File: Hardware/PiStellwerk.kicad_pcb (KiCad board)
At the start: 2 copper layers, 65 x 56 mm, 89 parts, among them J1 Conn_02x20_Odd_Even, J2 Screw_Terminal_01x02, J3 Screw_Terminal_01x02, J6 Conn_01x01, J7 Conn_01x04, J8 Conn_01x06, J9 Conn_01x05, Q1 Q_PMOS_GDS, U1 STM32F103C8Tx, U2 HT7533, U3 DRV8876, U4 SY8303, U5 ADUM4160, U6 ISO3088DW, U7 SY8303, U8 SY8303, U9 SY8303

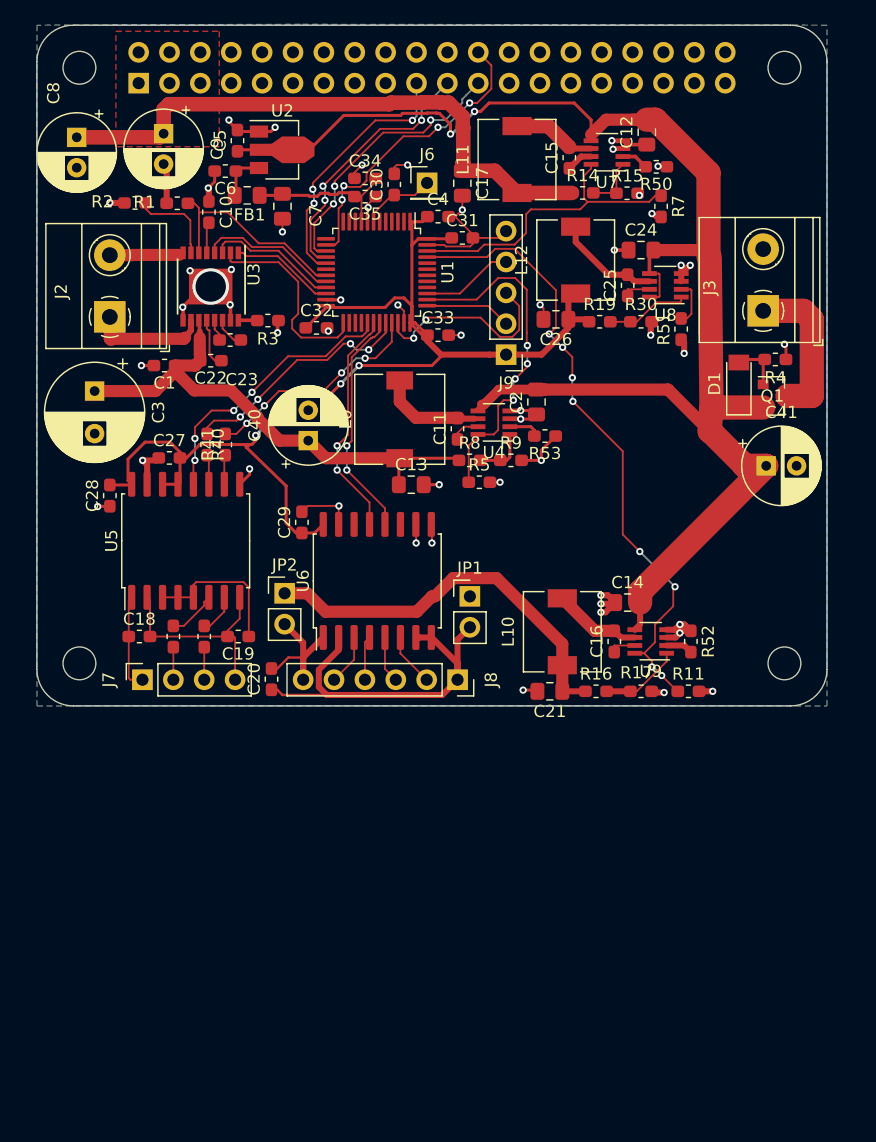
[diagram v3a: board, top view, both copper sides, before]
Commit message: initial work on 4layer design
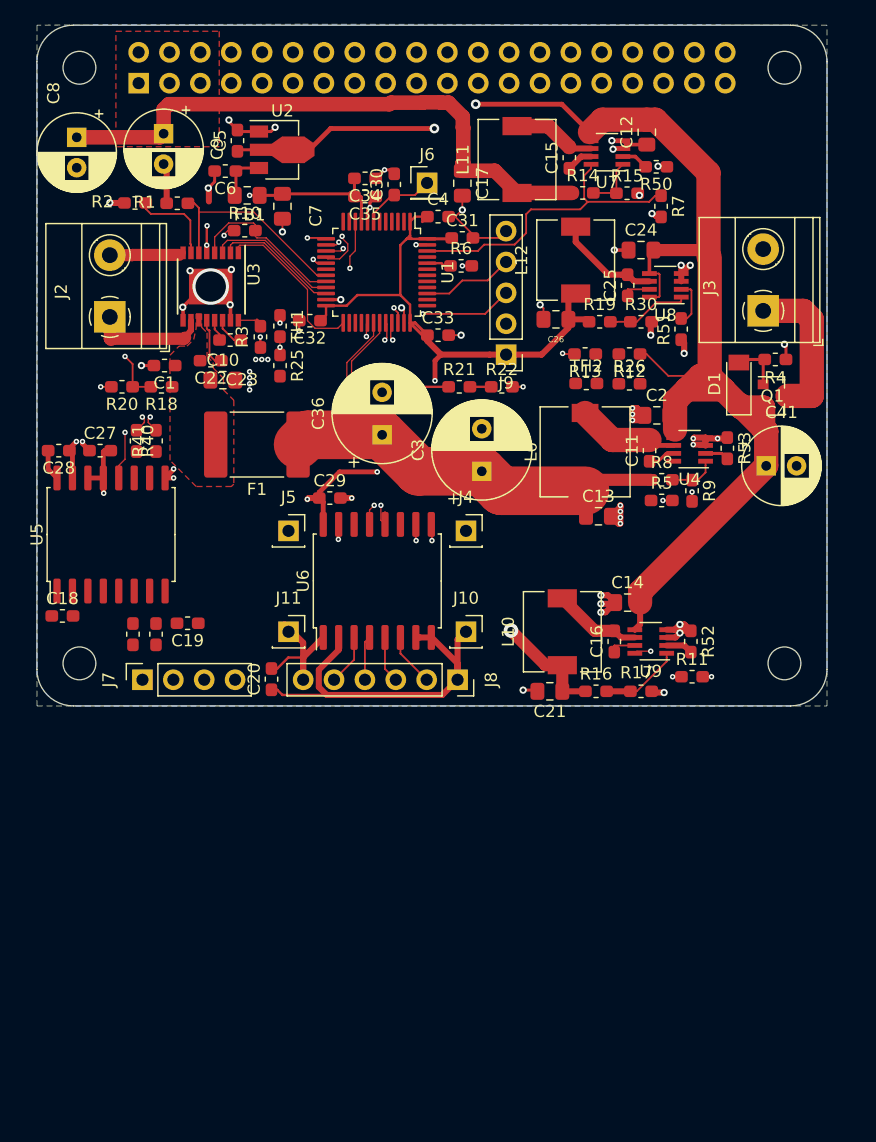
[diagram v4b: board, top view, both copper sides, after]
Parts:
- removed C40: 35V/100uF, Capacitor_THT:CP_Radial_D6.3mm_P2.50mm
- removed JP1, JP2: Jumper, Connector_PinHeader_2.54mm:PinHeader_1x02_P2.54mm_Vertical
- added C36: 35V/220uF, Capacitor_THT:CP_Radial_D8.0mm_P3.50mm, F.Cu at (28.4, 33.7)
- added F1: 24V/3A, Fuse:Fuse_2920_7451Metric, F.Cu at (18.1, 34.5)
- added J10: Conn_01x01, Connector_PinSocket_2.54mm:PinSocket_1x01_P2.54mm_Vertical, F.Cu at (35.3, 49.9)
- added J11: Conn_01x01, Connector_PinSocket_2.54mm:PinSocket_1x01_P2.54mm_Vertical, F.Cu at (20.7, 49.9)
- added J4: Conn_01x01, Connector_PinSocket_2.54mm:PinSocket_1x01_P2.54mm_Vertical, F.Cu at (35.3, 41.6)
- added J5: Conn_01x01, Connector_PinSocket_2.54mm:PinSocket_1x01_P2.54mm_Vertical, F.Cu at (20.7, 41.6)
- added R10: R, Resistor_SMD:R_0603_1608Metric_Pad1.05x0.95mm_HandSolder, F.Cu at (17.1, 16.9)
- added R12: R, Resistor_SMD:R_0603_1608Metric_Pad1.05x0.95mm_HandSolder, F.Cu at (48.8, 27.1)
- added R13: R, Resistor_SMD:R_0603_1608Metric_Pad1.05x0.95mm_HandSolder, F.Cu at (45.1, 27.1)
- added R18: R, Resistor_SMD:R_0603_1608Metric_Pad1.05x0.95mm_HandSolder, F.Cu at (10.2, 29.8)
- added R20: R, Resistor_SMD:R_0603_1608Metric_Pad1.05x0.95mm_HandSolder, F.Cu at (7.00, 29.8)
- added R21: R, Resistor_SMD:R_0603_1608Metric_Pad1.05x0.95mm_HandSolder, F.Cu at (34.8, 29.8)
- added R22: R, Resistor_SMD:R_0603_1608Metric_Pad1.05x0.95mm_HandSolder, F.Cu at (38.2, 29.8)
- added R25: R, Resistor_SMD:R_0603_1608Metric_Pad1.05x0.95mm_HandSolder, F.Cu at (20.0, 28.0)
- added R26: R, Resistor_SMD:R_0603_1608Metric_Pad1.05x0.95mm_HandSolder, F.Cu at (48.8, 29.5)
- added R6: 10K, Resistor_SMD:R_0603_1608Metric_Pad1.05x0.95mm_HandSolder, F.Cu at (34.9, 19.8)
- added TH1: Thermistor_NTC, Resistor_SMD:R_0603_1608Metric_Pad1.05x0.95mm_HandSolder, F.Cu at (20.0, 24.8)
- added TH2: Thermistor_NTC, Resistor_SMD:R_0603_1608Metric_Pad1.05x0.95mm_HandSolder, F.Cu at (45.2, 29.5)
- C10: value 35V/100nF -> 35V/10uF; footprint Capacitor_SMD:C_0603_1608Metric_Pad1.05x0.95mm_HandSolder -> Capacitor_SMD:C_0805_2012Metric_Pad1.15x1.40mm_HandSolder
- R1: value R -> 2K42
- moved C3 32.5 mm to (36.6, 36.7), turned to 90 degrees
- moved U4 16.2 mm to (53.7, 34.9)
- moved C11 15.9 mm to (50.4, 35.0)
- moved R8 15.9 mm to (51.4, 37.4)
- moved C13 15.6 mm to (46.2, 40.4)
- moved L0 15.5 mm to (45.1, 35.1)
- moved R9 15.1 mm to (53.9, 38.3), turned to 270 degrees
- moved R5 15.1 mm to (51.4, 39.1)
- moved R53 15.0 mm to (56.8, 34.8), turned to 270 degrees
- moved C10 13.9 mm to (15.3, 29.2), turned to 0 degrees
- moved C2 9.96 mm to (51.0, 32.1), turned to 0 degrees
- moved C18 6.55 mm to (2.10, 48.6)
- moved U5 6.16 mm to (6.10, 41.9)
- moved R40 5.81 mm to (8.20, 34.2)
- moved C27 5.73 mm to (5.20, 35.0)
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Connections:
- C1 pad 1: 18V -> 18V_FUSED
- C10 pad 1: GND -> 18V_FUSED
- C10 pad 2: +3V3 -> GND
- C22 pad 2: 18V -> 18V_FUSED
- U1 pad 10: (no net) -> NTC1_ADC
- U1 pad 11: (no net) -> ADC_IN1
- U1 pad 12: (no net) -> ADC_IN2
- U1 pad 13: (no net) -> ADC_IN3
- U1 pad 18: (no net) -> NTC2_ADC
- U1 pad 22: IN1 -> IN2
- U1 pad 25: IN2 -> IN1
- U1 pad 44: (no net) -> Net-(R6-Pad1)
- U3 pad 11: 18V -> 18V_FUSED
- U3 pad 5: +3V3 -> 3VA3
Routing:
- net EN_SEC_5V: track 52.8 -> 5.60 mm, vias 8 -> 2
- net ADC_IN3: track 0.00 -> 39.1 mm, vias 0 -> 2
- net ENABLE_18V: track 28.5 -> 0.00 mm, vias 4 -> 0
- net 3VA3: track 12.8 -> 35.6 mm, vias 0 -> 4
- net /USB_GND: track 17.5 -> 0.00 mm
- net NTC1_ADC: track 0.00 -> 14.4 mm, vias 0 -> 2
- net /USB_VDD: track 12.4 -> 0.00 mm
- net /USB+: track 7.93 -> 0.00 mm
- net USB_D+: track 18.4 -> 25.6 mm, vias 4 -> 2
- net SWCLK: track 7.10 -> 0.00 mm
- net USB_PIN: track 22.9 -> 29.3 mm, vias 4 -> 2
- net 3V3: track 104.6 -> 98.4 mm
- net IN2: track 16.5 -> 10.3 mm
- net USB_D-: track 19.7 -> 25.6 mm, vias 4 -> 2
- net IN1: track 8.60 -> 13.7 mm
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- added copper zone on F.Cu, net 18V_FUSED
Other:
- copper layers 2 -> 4
- net class 90 Ohms JLC7628 added: clearance 0.1016, trace_width 0.117602, via_dia 0.45, via_drill 0.2
- net class Default: clearance 0.1524 -> 0.1; trace_width 0.1524 -> 0.1; via_dia 0.6 -> 0.45; via_drill 0.3 -> 0.2
- rule trace_clearance: 0.1524 -> 0.1
- rule via_min_drill: 0.3 -> 0.2
- rule via_min_size: 0.6 -> 0.45

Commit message: finalize first draft for 4layer board
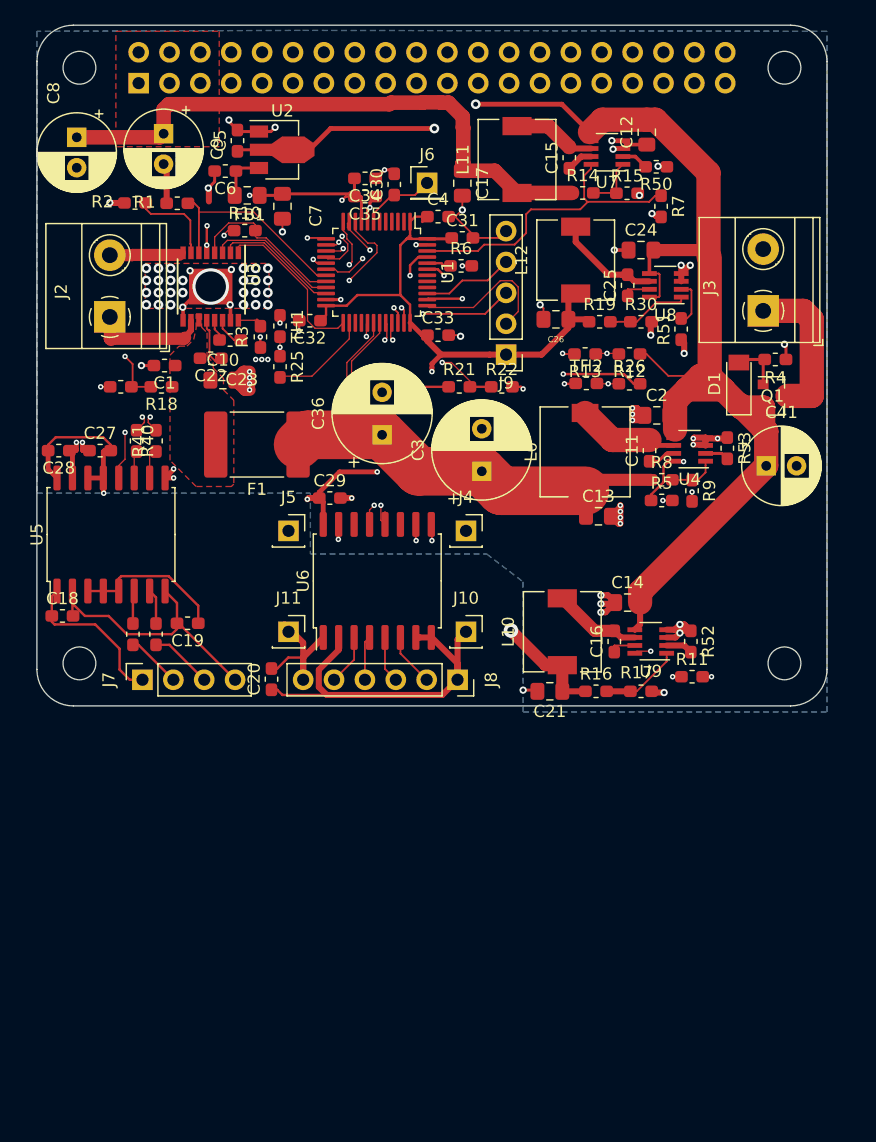
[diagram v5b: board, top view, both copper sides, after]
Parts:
- moved C22 0.20 mm to (14.3, 27.4)
- moved R25 0.10 mm to (20.0, 28.1)
- moved R20 0.10 mm to (6.90, 29.8)
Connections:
- R25 pad 2: NTC_EN -> NTC1_EN
- R26 pad 2: NTC_EN -> NTC2_EN
- U1 pad 26: (no net) -> NTC1_EN
- U1 pad 43: (no net) -> NTC2_EN
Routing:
- net EN_SEC_5V: track 5.60 -> 47.3 mm, vias 2 -> 3
- net ENABLE_18V: track 0.00 -> 34.4 mm, vias 0 -> 2
- net NTC2_ADC: track 0.00 -> 30.4 mm, vias 0 -> 2
- net 3VA3: track 35.6 -> 64.7 mm, vias 4 -> 6
- net ADC_IN1: track 0.00 -> 28.1 mm, vias 0 -> 2
- net NTC2_EN: track 0.00 -> 24.3 mm, vias 0 -> 2
- net /USB_GND: track 0.00 -> 23.2 mm
- net ADC_IN2: track 1.75 -> 20.9 mm, vias 0 -> 2
- net /USB+: track 0.00 -> 13.1 mm
- net /USB_VDD: track 0.00 -> 12.6 mm
- net SWCLK: track 0.00 -> 12.1 mm
- net NTC1_EN: track 0.00 -> 8.29 mm
- net GND: track 102.0 -> 108.1 mm, vias 72 -> 98
- net Net-(J7-Pad3): track 0.00 -> 5.16 mm
- net Net-(J7-Pad2): track 0.00 -> 4.52 mm
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- added copper zone on F.Cu, net GND

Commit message: Remove messy item references from silkscreen, add gerberfiles to gitignore
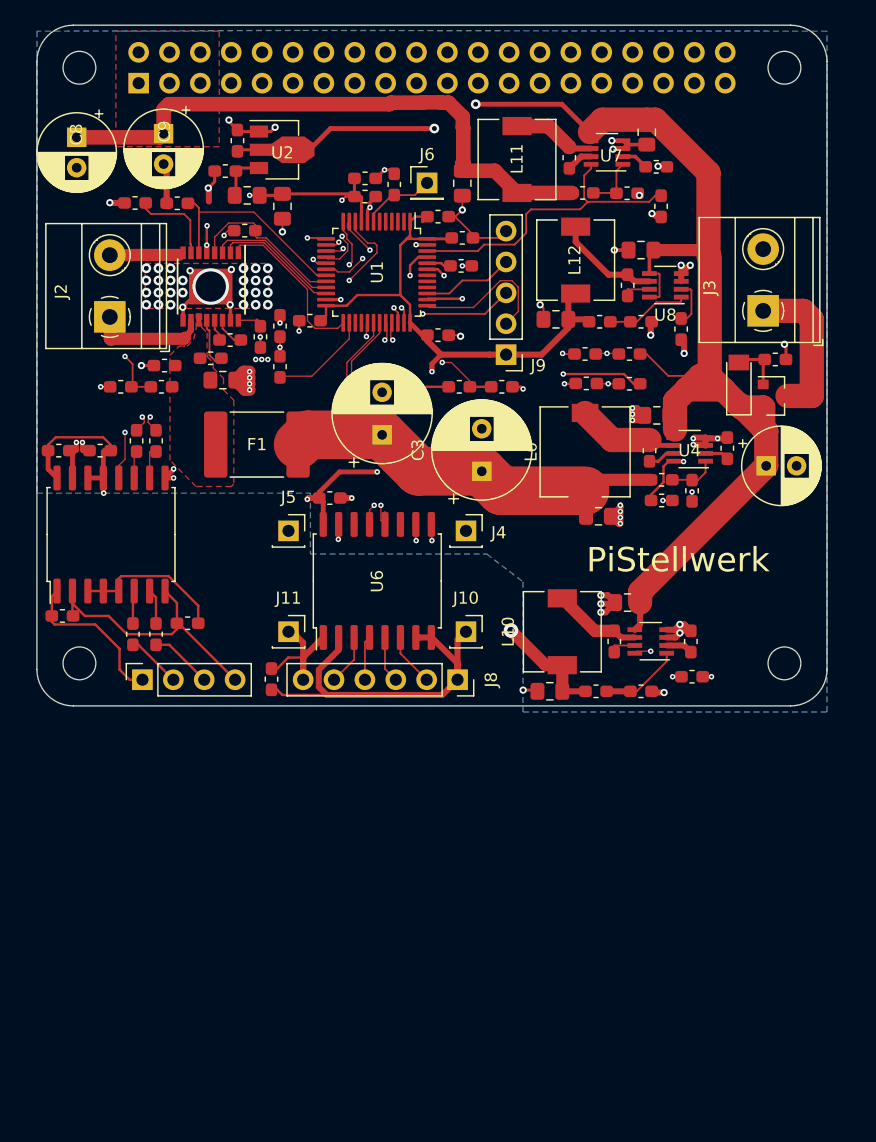
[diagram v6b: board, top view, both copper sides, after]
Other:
- board text added: "PiStellwerk"
